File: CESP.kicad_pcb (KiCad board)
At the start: 2 copper layers, 55.9 x 44.7 mm, 8 parts

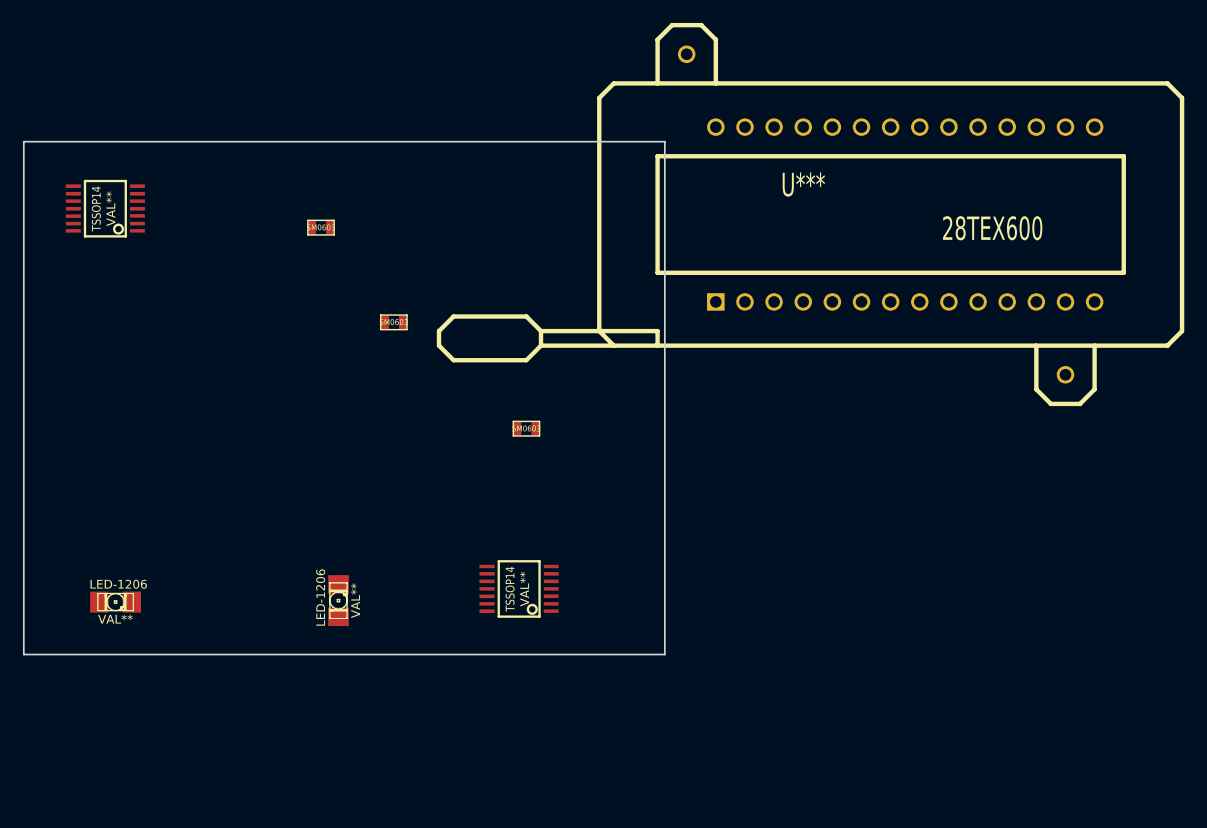
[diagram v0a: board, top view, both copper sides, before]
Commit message: Revert "Added large footprint"
This reverts commit b333fd873bfd8b188279f3009577f26e7c66da37.
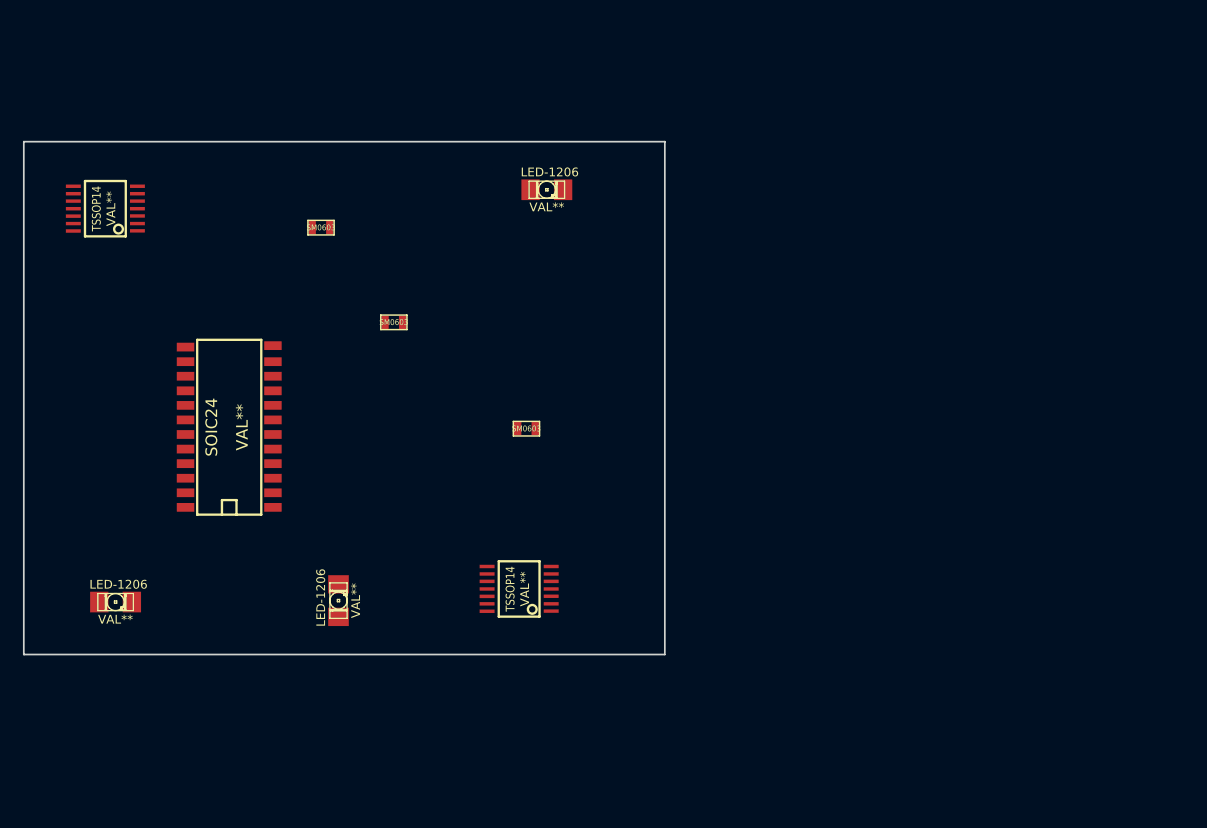
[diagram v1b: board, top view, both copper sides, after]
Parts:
- removed U***: 28TEX600, 28tex600
- added LED-1206: VAL**, LED-1206, F.Cu at (201.5, 99.9)
- added SOIC24: VAL**, SOIC24, F.Cu at (173.9, 120.7)

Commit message: First draft of schematic
First draft of having added and connected items in the schematic,
annotated and sized the devices and added a netlist.
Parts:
- removed LED-1206 (x3): VAL**, LED-1206
- removed SM0603 (x3): Val**, SM0603
- removed SOIC24: VAL**, SOIC24
- removed TSSOP14 (x2): VAL**, TSSOP14
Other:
- board outline removed
- board text removed: "NOTE: THIS IS JUST A TEST BOARD REMOVE ALL COMPONENTS AND CREATE YOUR OWN INCLUDE SCHEMATIC HOOKUPS/NETLIST"

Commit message: First draft of PCB layout
It's a total mess, but I got it to pass ERC, have the 7805 connected,
used a bunch of different foot prints, used vias and successfully beat
my head against the brickwall of KiCad.
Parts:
- added C1: .1µF, SM0805, F.Cu at (192.3, 149.9)
- added C2: .1µF, SM0805, F.Cu at (207.3, 130.8)
- added C3: 1µF, SM0805, F.Cu at (207.5, 149.9)
- added C4: 10µF, SM0805, F.Cu at (207.5, 147.1)
- added C5: .1µF, SM0805, F.Cu at (192.8, 146.1)
- added C6: .33µF, SM0805, B.Cu at (193.0, 134.6)
- added C7: .01µF, SM0805, B.Cu at (206.4, 134.6)
- added K1: CONN_3, SIL-3, F.Cu at (200.0, 130.8)
- added R1: 68K, SM1206, F.Cu at (201.9, 138.4)
- added R2: 1K, SM0805, F.Cu at (206.5, 141.2)
- added R3: 1K, SM0805, F.Cu at (210.1, 142.7)
- added R4: 10K, SM1206, F.Cu at (200.9, 143.5)
- added R5: 1K, SM0805, F.Cu at (201.2, 147.6)
- added R6: 2K2, SM1206, F.Cu at (194.3, 142.2)
- added U1: 7555, SO8E, F.Cu at (208.3, 135.9)
- added U2: LM741, SO8E, F.Cu at (194.8, 136.1)
- added U3: 7805-REG, DPAK3, B.Cu at (200.0, 138.4)
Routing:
- net N-000005: track 0.00 -> 44.2 mm, vias 0 -> 2
- net GND: track 0.00 -> 37.4 mm, vias 0 -> 5
- net N-000008: track 0.00 -> 35.9 mm, vias 0 -> 2
- net N-000007: track 0.00 -> 17.8 mm
- net N-0000011: track 0.00 -> 16.7 mm
- net N-0000010: track 0.00 -> 13.7 mm
- net N-000006: track 0.00 -> 10.9 mm
- net VCC: track 0.00 -> 9.07 mm, vias 0 -> 1
- net N-0000014: track 0.00 -> 8.95 mm, vias 0 -> 2
- net N-0000013: track 0.00 -> 8.75 mm
- net N-0000012: track 0.00 -> 3.86 mm
- net N-000009: track 0.00 -> 3.71 mm
- net -9V: track 0.00 -> 3.43 mm
- net (no net): track 0.00 -> 2.35 mm
- added copper zone on B.Cu, net GND
- added copper zone on F.Cu, net VCC

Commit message: Several PCB layout drafts later...
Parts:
- moved R3 21.8 mm to (189.4, 135.9)
- moved C2 19.7 mm to (191.1, 142.1), turned to 270 degrees
- moved C3 18.2 mm to (189.6, 146.8), turned to 270 degrees
- moved U1 15.2 mm to (193.0, 135.9), turned to 180 degrees
- moved C4 15.1 mm to (192.4, 146.8), turned to 270 degrees
- moved R6 13.4 mm to (207.6, 143.0), turned to 90 degrees
- moved C5 13.0 mm to (205.1, 142.0), turned to 90 degrees
- moved U2 12.2 mm to (207.0, 135.9), turned to 180 degrees
- moved R4 9.79 mm to (194.1, 150.5), turned to 180 degrees
- moved R2 9.61 mm to (198.1, 136.5), turned to 270 degrees
- moved C1 7.85 mm to (193.5, 142.1)
- moved R5 5.64 mm to (195.6, 146.8), turned to 0 degrees
- moved R1 5.29 mm to (197.6, 141.5), turned to 180 degrees
- moved C7 3.86 mm to (205.7, 138.4)
- moved C6 3.81 mm to (193.0, 138.4)
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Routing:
- net N-0000010: track 13.7 -> 42.6 mm, vias 0 -> 1
- net N-000008: track 35.9 -> 11.5 mm, vias 2 -> 0
- net N-000007: track 17.8 -> 2.48 mm
- net N-000005: track 44.2 -> 31.9 mm, vias 2 -> 0
- net N-000006: track 10.9 -> 3.32 mm
- net N-0000013: track 8.75 -> 2.73 mm
- net VCC: track 9.07 -> 15.1 mm, vias 1 -> 0
- net N-0000011: track 16.7 -> 11.2 mm
- net -9V: track 3.43 -> 8.62 mm
- net N-0000014: track 8.95 -> 11.9 mm, vias 2 -> 0
- net (no net): track 2.35 -> 0.00 mm
- net N-0000012: track 3.86 -> 2.60 mm
- net GND: track 37.4 -> 36.6 mm, vias 5 -> 3
- net N-000009: track 3.71 -> 4.35 mm
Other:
- rule trace_min: 0.254 -> 0.1524
- rule via_min_drill: 0.508 -> 0.3302
- rule via_min_size: 0.889 -> 0.508

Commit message: And yet further PCB layout drafts...
... I'm beginning to truly despise this board.  I think it has it out
for me.
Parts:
- moved C6 31.5 mm to (223.4, 146.7), turned to 270 degrees
- moved U3 24.1 mm to (223.4, 140.8), turned to 90 degrees
- moved U1 22.9 mm to (215.8, 133.5)
- moved C3 19.6 mm to (202.3, 131.8)
- moved K1 18.7 mm to (215.8, 140.8)
- moved C7 18.0 mm to (223.4, 135.0), turned to 90 degrees
- moved R4 17.7 mm to (209.7, 142.2), turned to 90 degrees
- moved R3 17.3 mm to (205.9, 130.8), turned to 180 degrees
- moved C2 16.8 mm to (207.3, 137.4), turned to 180 degrees
- moved C1 15.6 mm to (207.3, 134.7), turned to 180 degrees
- moved U2 15.1 mm to (215.8, 148.2)
- moved R1 14.8 mm to (210.8, 134.7), turned to 270 degrees
- moved C4 14.4 mm to (202.3, 136.4)
- moved R2 13.6 mm to (210.4, 130.8), turned to 180 degrees
- moved C5 10.6 mm to (210.9, 150.9), turned to 0 degrees
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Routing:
- net N-0000010: track 42.6 -> 19.0 mm
- net N-000005: track 31.9 -> 13.2 mm
- net N-000008: track 11.5 -> 21.6 mm, vias 0 -> 2
- net N-0000013: track 2.73 -> 9.93 mm
- net N-000009: track 4.35 -> 11.1 mm
- net VCC: track 15.1 -> 9.37 mm
- net N-0000012: track 2.60 -> 7.73 mm
- net -9V: track 8.62 -> 4.96 mm
- net N-0000014: track 11.9 -> 9.73 mm
- net N-000006: track 3.32 -> 5.50 mm
- net GND: track 36.6 -> 35.2 mm
- net N-0000011: track 11.2 -> 10.4 mm
- net N-000007: track 2.48 -> 1.97 mm
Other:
- board outline added: 39.4 x 25.4 mm

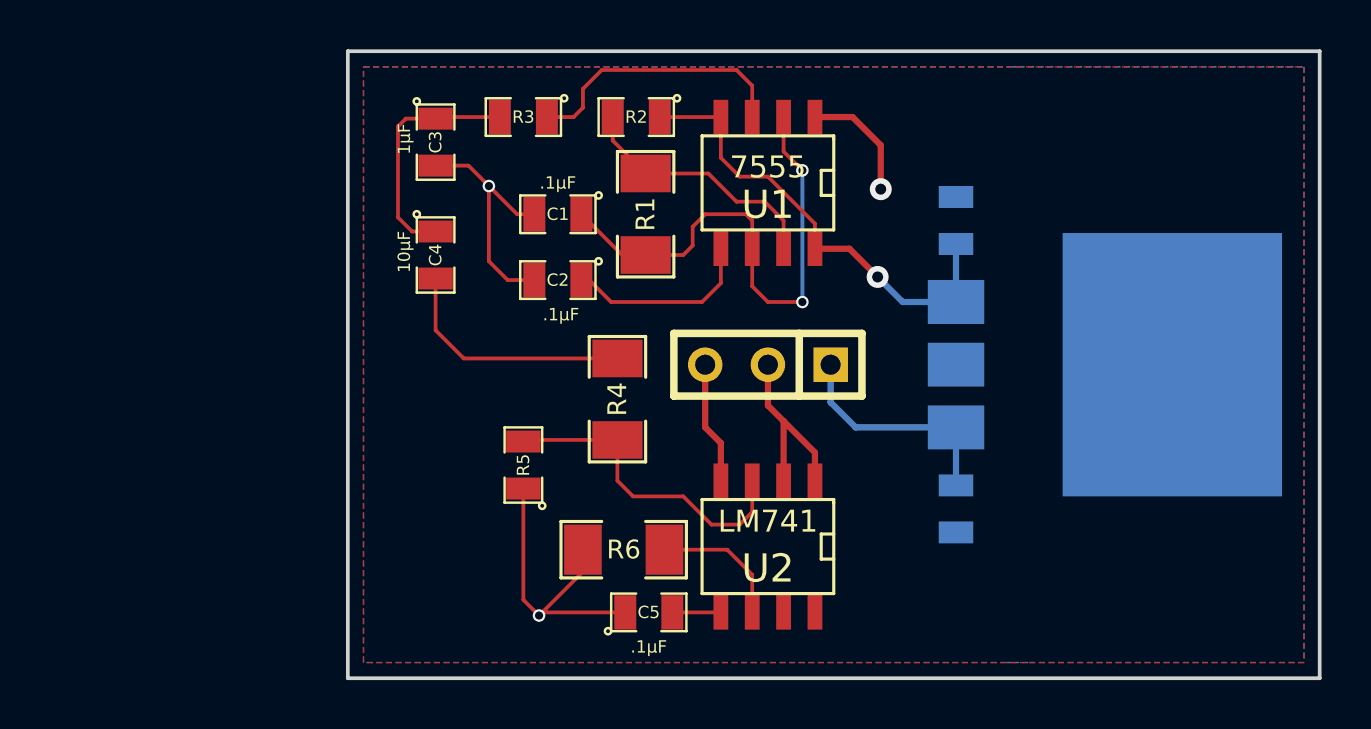
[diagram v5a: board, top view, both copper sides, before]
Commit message: Added headers and SPI vs SPI logo...
Headers added to allow customizing the Signal and Feedback resistors.

Headers added to allow measurement with an oscilloscope.

SPI vs. SPI logo from John Lohe added.
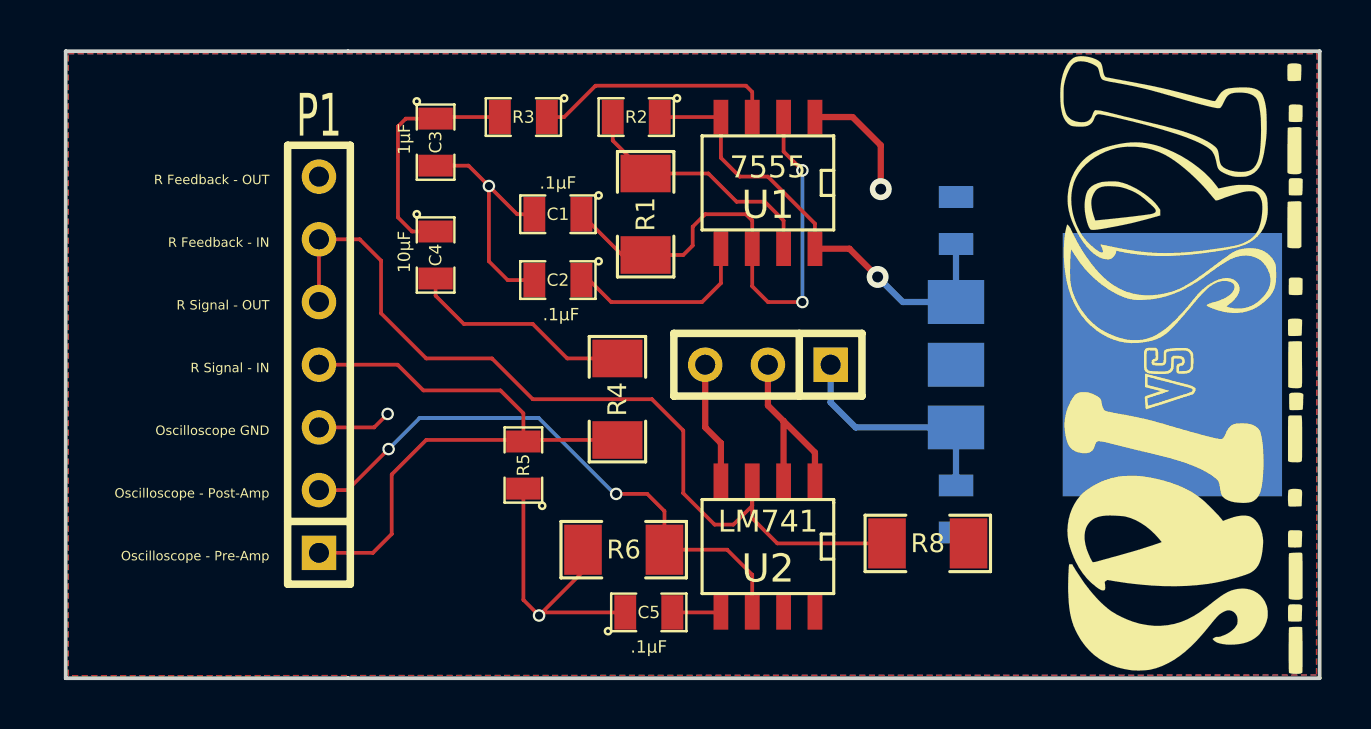
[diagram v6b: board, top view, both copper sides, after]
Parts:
- added P1: CONN_7, SIL-7, F.Cu at (197.6, 140.8)
- added R8: 270K, SM1206, F.Cu at (222.2, 148.1)
- added VAL: SPIvsSPI_1, SPIvsSPI_1000, F.Cu at (232.5, 140.8)
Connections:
- R4 pad 1: N-000005 -> N-000004
- R5 pad 2: N-000005 -> N-000004
- U2 pad 3: N-000005 -> N-000003
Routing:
- net N-000003: track 0.00 -> 31.9 mm
- net N-000004: track 0.00 -> 25.7 mm
- net N-000008: track 5.50 -> 23.8 mm, vias 0 -> 2
- net N-000005: track 13.2 -> 0.00 mm
- net N-000006: track 0.00 -> 4.44 mm
- net GND: track 35.2 -> 38.2 mm, vias 3 -> 4
- net N-0000014: track 11.1 -> 9.97 mm
- net N-000009: track 9.93 -> 9.12 mm
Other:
- board size 39.4 x 25.4 mm -> 50.8 x 25.4 mm
- board text added: "Oscilloscope - Post-Amp"
- board text added: "Oscilloscope - Pre-Amp"
- board text added: "Oscilloscope GND"
- board text added: "R Feedback - IN"
- board text added: "R Feedback - OUT"
- board text added: "R Signal - IN"
- board text added: "R Signal - OUT"

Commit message: Revised logo...
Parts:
- removed the VAL at (232.5, 140.8)
- added VAL: SPIvsSPI_1, SPIvsSPI_500, F.Cu at (232.2, 140.8)

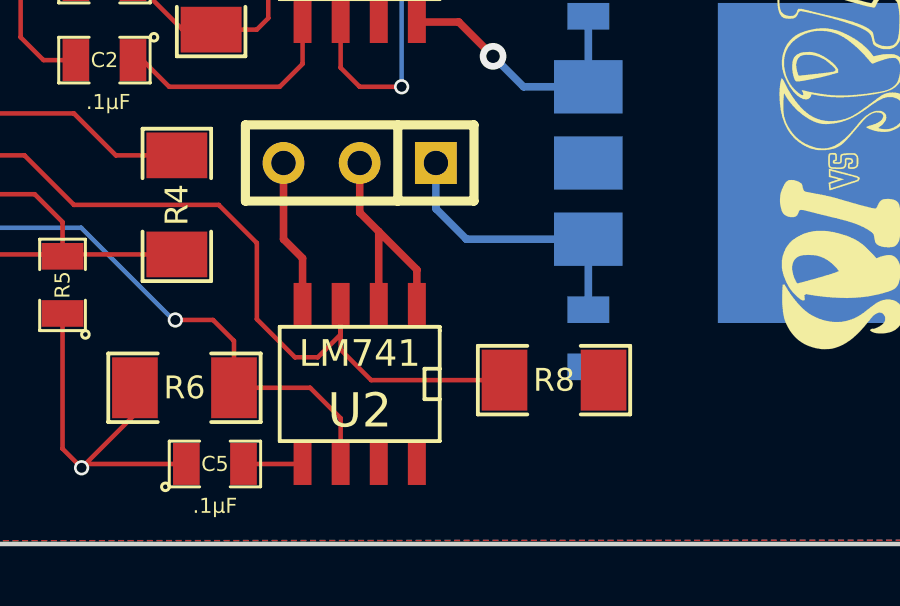
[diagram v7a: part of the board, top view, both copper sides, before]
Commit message: Removed old components...
There was a resistor left over that has been replaced by headers.  The
board passes DRC now.
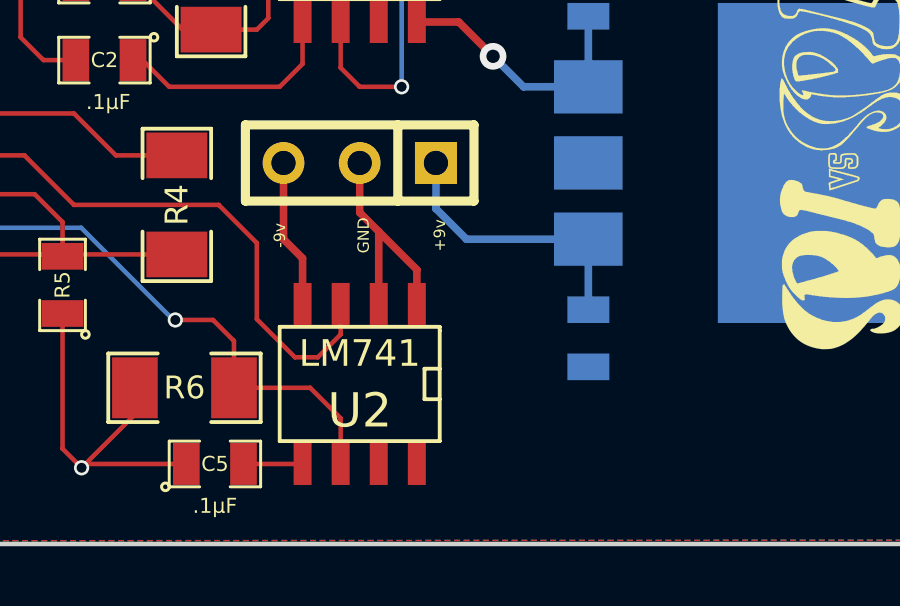
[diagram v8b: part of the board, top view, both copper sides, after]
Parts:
- removed R8: 270K, SM1206
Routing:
- net N-000006: track 4.44 -> 0.00 mm
- net N-000003: track 31.9 -> 28.9 mm
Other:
- board text added: "+9v"
- board text added: "-9v"
- board text added: "GND"
